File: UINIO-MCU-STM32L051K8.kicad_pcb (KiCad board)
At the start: 2 copper layers, 48.3 x 20.3 mm, 32 parts, among them J1 Conn_01x14_Pin, J2 Conn_01x14_Pin, J3 Conn_01x04_Pin, SW1 SW_Push, SW2 SW_Push, U1 ME6211, U2 W25Q128JVSSIQ, U3 STM32L051K8U6, Y1 Crystal-FC135-32.768

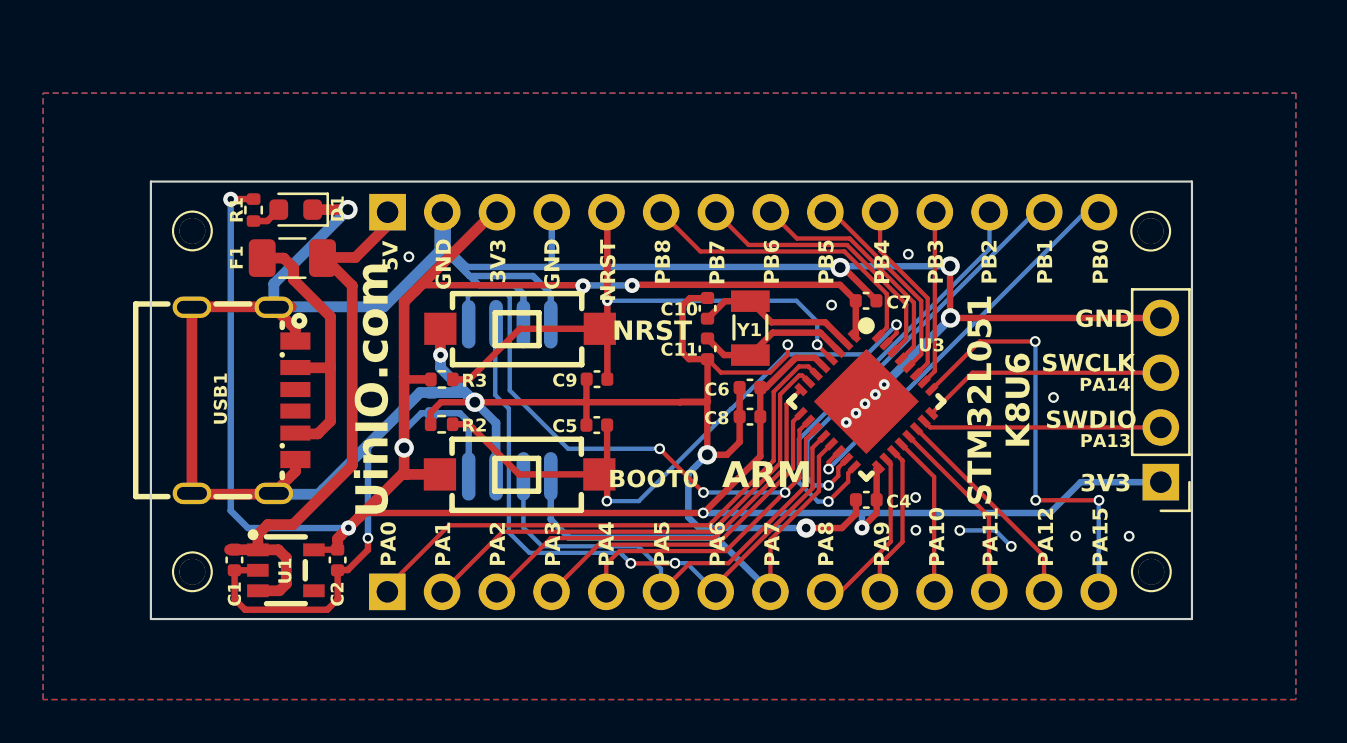
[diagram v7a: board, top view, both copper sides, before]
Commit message: Release UINIO-MCU-STM32L051K8 version 3.3.0.
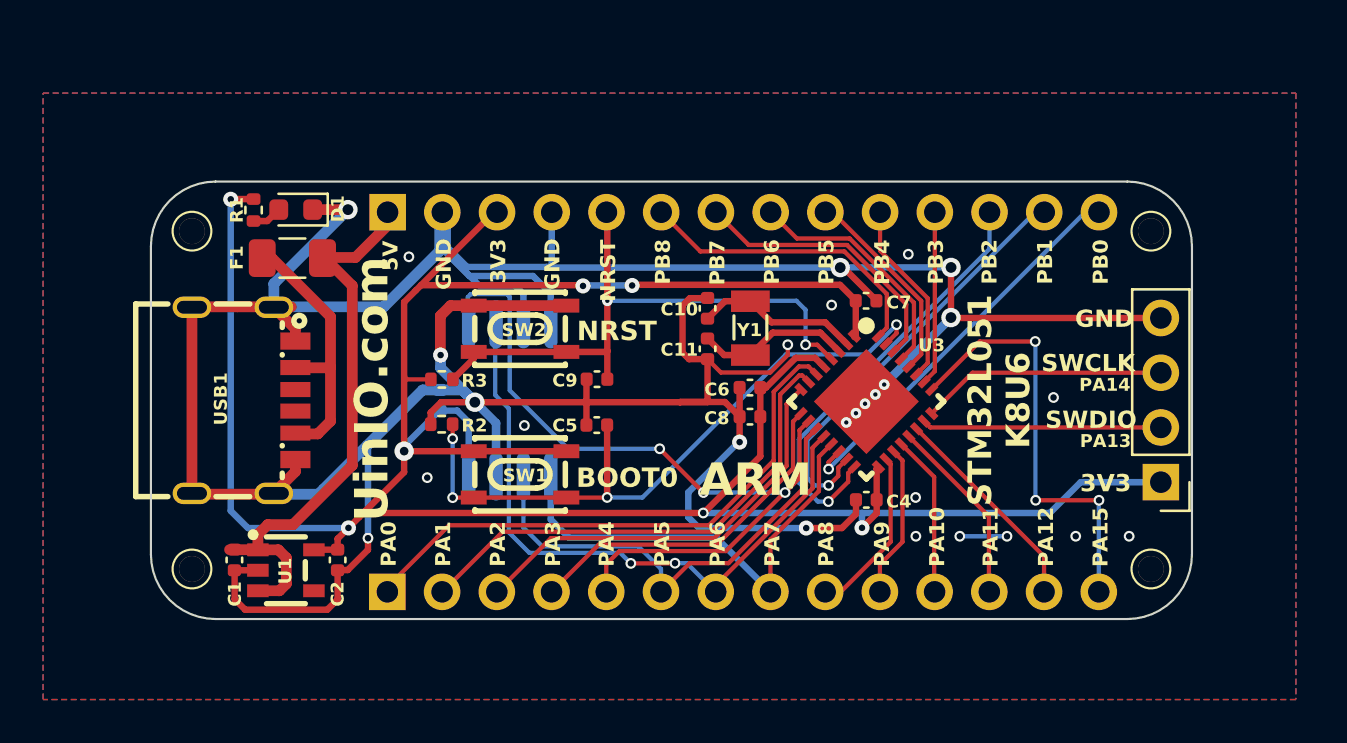
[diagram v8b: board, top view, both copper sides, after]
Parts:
- removed the ? at (135.4, 103.7)
- removed the ? at (156.4, 103.7)
- added ?: LOGO, LOGO, B.Cu at (135.3, 103.7)
- added ?: LOGO, LOGO, B.Cu at (156.4, 103.8)
- SW1: value SW_Push -> Boot选择按键; footprint Uinio:SW-SMD_L6.0-W3.3-LS8.0-1 -> Uinio:KEY-SMD_4P-L4.2-W3.4-P2.15-LS4.7
- SW2: value SW_Push -> 复位按键; footprint Uinio:SW-SMD_L6.0-W3.3-LS8.0-1 -> Uinio:KEY-SMD_4P-L4.2-W3.4-P2.15-LS4.7
- moved C3 0.40 mm to (139.0, 103.7)
- moved Hole1 0.13 mm to (172.0, 111.5)
- moved Hole4 0.13 mm to (127.5, 111.5)
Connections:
- SW1 pad 2: /BOOT0 -> /VDD_3.3V
- SW2 pad 2: /NRST -> GND
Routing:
- net /VDD_3.3V: track 125.8 -> 131.5 mm
- net GND: track 188.3 -> 193.3 mm, vias 25 -> 27
- net /BOOT0: track 28.5 -> 31.8 mm, vias 2 -> 4
- net /NRST: track 27.1 -> 28.2 mm
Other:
- outline, holes or cut-outs redrawn
